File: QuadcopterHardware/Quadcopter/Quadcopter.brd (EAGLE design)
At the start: 3 x 47 mm, 47 parts, among them J2 FTDI_DEVICERA_SMT, M1 WIRELESS-NRF24L01, U1 ATMEGA328P_TQFP, U3 GY-521MPU6050

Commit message: more work on the board
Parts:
- C10, C11, C12, C13, C8: device rcl:C1206 -> rcl:C1210
- moved C2 115.4 mm to (38.7, 12.5)
- moved C1 113.1 mm to (43.0, 16.2), turned to 270 degrees
- moved MOSFET4 103.9 mm to (39.8, 3.59), turned to 180 degrees
- moved C13 100.8 mm to (38.2, 8.55)
- moved MOSFET3 89.2 mm to (31.1, 3.59), turned to 180 degrees
- moved C12 86.3 mm to (29.5, 8.55)
- moved C11 72.6 mm to (20.9, 8.55)
- moved C8 67.5 mm to (38.2, 22.1), turned to 90 degrees
- moved FLYBACK_DIODE4 51.8 mm to (34.1, 3.58), flipped to the bottom
- moved U3 48.8 mm to (24.4, 15.2), flipped to the bottom, turned to 270 degrees
- moved FLYBACK_DIODE3 46.9 mm to (25.6, 3.58), flipped to the bottom
- moved MOTOR3 46.6 mm to (36.2, 3.64)
- moved MOTOR2 41.9 mm to (27.6, 3.64)
- moved U$2 38.1 mm to (42.7, 21.2), turned to 180 degrees
- moved FLYBACK_DIODE2 31.8 mm to (16.8, 3.33), flipped to the bottom
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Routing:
- net GND: track 3.67 -> 30.8 mm, vias 0 -> 1
- net VBATT: track 9.88 -> 21.5 mm
- net XTAL2: track 4.49 -> 0.00 mm
- net XTAL1: track 3.88 -> 0.00 mm
- net 3V3: track 0.00 -> 3.03 mm
- net DRAIN3: track 3.32 -> 5.82 mm
- net AREF: track 2.89 -> 0.75 mm, vias 0 -> 1
- net DRAIN4: track 3.36 -> 2.32 mm
- net DRAIN1: track 6.85 -> 5.95 mm
- net DRAIN2: track 6.81 -> 6.07 mm
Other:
- board size 3 x 47 mm -> 47 x 28 mm

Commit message: more work on board
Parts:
- moved C6 76.6 mm to (5.15, 12.7), turned to 270 degrees
- moved R6 73.9 mm to (8.55, 12.0)
- moved S1 58.0 mm to (3.90, 7.15), turned to 270 degrees
- flipped J2 to the bottom, turned to 90 degrees
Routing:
- net AREF: track 0.75 -> 0.00 mm, vias 1 -> 0
- net GND: track 30.8 -> 30.3 mm, vias 1 -> 0
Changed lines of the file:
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@@
 <element name="C4" library="rcl" package="C0603" value="100nF" x="-41.91" y="57.15"/>
 <element name="C5" library="rcl" package="C0603" value="100nF" x="-49.53" y="57.15"/>
-<element name="C6" library="rcl" package="C0603" value="100nF" x="-57.15" y="57.15"/>
+<element name="C6" library="rcl" package="C0603" value="100nF" x="5.15" y="12.65" rot="R270"/>
 <element name="C7" library="rcl" package="C0603" value="100nF" x="30.85" y="16.73" rot="R90"/>
 <element name="C8" library="rcl" package="C1210" value="100uF" x="38.2" y="22.14" rot="R90"/>
@@
 <element name="FLYBACK_DIODE3" library="quad" package="MINI2-F3-B" value="DB2W40300L" x="25.6" y="3.58" rot="MR0"/>
 <element name="FLYBACK_DIODE4" library="quad" package="MINI2-F3-B" value="DB2W40300L" x="34.14" y="3.58" rot="MR0"/>
-<element name="J2" library="quad" package="FTDI_DEVICE_RA_SMT" value="FTDI_DEVICERA_SMT" x="-2.02" y="17.13" rot="R270">
-<attribute name="PROD_ID" value="CONN-08971" x="-2.02" y="17.13" size="1.778" layer="27" rot="R270" display="off"/>
+<element name="J2" library="quad" package="FTDI_DEVICE_RA_SMT" value="FTDI_DEVICERA_SMT" x="-2.02" y="17.12" rot="MR90">
+<attribute name="PROD_ID" value="CONN-08971" x="-2.02" y="17.12" size="1.778" layer="28" rot="MR90" display="off"/>
 </element>
 <element name="LED1" library="led" package="CHIP-LED0603" value="RED" x="85.76" y="25.92" rot="R270"/>
@@
 <element name="R3" library="rcl" package="R0603" value="150" x="88.91" y="22.58"/>
 <element name="R4" library="rcl" package="R0603" value="150" x="88.83" y="18.08"/>
-<element name="R6" library="rcl" package="R0603" value="10K" x="-44.45" y="63.5"/>
+<element name="R6" library="rcl" package="R0603" value="10K" x="8.55" y="12"/>
 <element name="R7" library="rcl" package="R0603" value="10K" x="-49.53" y="63.5"/>
 <element name="R8" library="rcl" package="R0603" value="1K" x="-30.48" y="68.58"/>
 <element name="R9" library="rcl" package="R0603" value="1.7K" x="-29.21" y="63.5"/>
 <element name="RES1" library="quad" package="CSTCE16M0V53-R0" value="CSTCE10M0G55-R0" x="31.03" y="9.63" rot="MR180"/>
-<element name="S1" library="quad" package="TACTILE-SWITCH-SMD" value="SWITCH-MOMENTARY-2SMD" x="-25.4" y="57.15">
-<attribute name="PROD_ID" value="SWCH-08247" x="-25.4" y="57.15" size="1.778" layer="27" display="off"/>
+<element name="S1" library="quad" package="TACTILE-SWITCH-SMD" value="SWITCH-MOMENTARY-2SMD" x="3.9" y="7.15" rot="R270">
+<attribute name="PROD_ID" value="SWCH-08247" x="3.9" y="7.15" size="1.778" layer="27" rot="R270" display="off"/>
 </element>
 <element name="U$1" library="quad" package="SOT95P270X145-5N" value="MCP1802T-3302I/OT" x="38.33" y="16.09" smashed="yes" rot="R180">
@@
 <wire x1="39.58" y1="12.5" x2="40.16" y2="12.5" width="1.016" layer="1"/>
 <wire x1="40.16" y1="12.5" x2="43" y2="15.34" width="1.016" layer="1"/>
-<wire x1="20.1574" y1="12.71" x2="30.48" y2="17.21" width="0" layer="19" extent="1-16"/>
-<wire x1="30.48" y1="17.21" x2="30.85" y2="17.58" width="0.4064" layer="1"/>
 <wire x1="13.67" y1="8.55" x2="13.67" y2="6.67" width="1.016" layer="1"/>
 <wire x1="13.67" y1="6.67" x2="13" y2="6" width="1.016" layer="1"/>
@@
 <wire x1="42.74" y1="22.2" x2="41.41" y2="16.09" width="0" layer="19" extent="1-1"/>
 <wire x1="30.93" y1="6.43" x2="39" y2="5.75" width="0" layer="19" extent="1-1"/>
-<wire x1="22.3" y1="6.8" x2="30.25" y2="5.75" width="0" layer="19" extent="1-1"/>
-<wire x1="31.03" y1="9.63" x2="22.3" y2="8.55" width="0" layer="19" extent="1-1"/>
-<wire x1="28.7426" y1="11.91" x2="31.03" y2="9.63" width="0" layer="19" extent="1-1"/>
-<wire x1="28.7426" y1="13.51" x2="28.7426" y2="11.91" width="0" layer="19" extent="1-1"/>
-<wire x1="18.04" y1="24.1" x2="28.7426" y2="13.51" width="0" layer="19" extent="1-1"/>
-<wire x1="13.67" y1="8.55" x2="31.03" y2="9.63" width="0" layer="19" extent="1-1"/>
-<wire x1="20.1574" y1="12.71" x2="28.7426" y2="11.91" width="0" layer="19" extent="1-1"/>
-<wire x1="8.63" y1="24.99" x2="18.04" y2="24.1" width="0" layer="19" extent="1-1"/>
-<wire x1="2.98" y1="10.78" x2="13.67" y2="8.55" width="0" layer="19" extent="1-1"/>
-<wire x1="2.98" y1="13.32" x2="2.98" y2="10.78" width="0" layer="19" extent="1-1"/>
-<wire x1="-16.93" y1="63.5" x2="8.63" y2="24.99" width="0" layer="19" extent="1-1"/>
+<wire x1="31.03" y1="9.63" x2="30.93" y2="8.55" width="0" layer="19" extent="1-16"/>
+<wire x1="28.7426" y1="11.91" x2="31.03" y2="9.63" width="0" layer="19" extent="16-16"/>
+<wire x1="28.7426" y1="13.51" x2="28.7426" y2="11.91" width="0" layer="19" extent="16-16"/>
+<wire x1="30.85" y1="17.58" x2="28.7426" y2="13.51" width="0" layer="19" extent="1-16"/>
+<wire x1="22.3" y1="8.55" x2="28.7426" y2="11.91" width="0" layer="19" extent="1-16"/>
+<wire x1="20.1574" y1="12.71" x2="22.3" y2="8.55" width="0" layer="19" extent="1-16"/>
+<wire x1="13.67" y1="8.55" x2="20.1574" y2="12.71" width="0" layer="19" extent="1-16"/>
+<wire x1="5.805" y1="9.944" x2="13.67" y2="8.55" width="0" layer="19" extent="1-1"/>
+<wire x1="2.98" y1="20.93" x2="5.805" y2="9.944" width="0" layer="19" extent="1-16"/>
+<wire x1="2.98" y1="23.47" x2="2.98" y2="20.93" width="0" layer="19" extent="16-16"/>
+<wire x1="8.63" y1="24.99" x2="2.98" y2="23.47" width="0" layer="19" extent="16-16"/>
+<wire x1="18.04" y1="24.1" x2="8.63" y2="24.99" width="0" layer="19" extent="1-1"/>
+<wire x1="-16.93" y1="63.5" x2="2.98" y2="23.47" width="0" layer="19" extent="1-16"/>
 <wire x1="-23.28" y1="63.5" x2="-16.93" y2="63.5" width="0" layer="19" extent="1-1"/>
-<wire x1="-28.194" y1="59.055" x2="-23.28" y2="63.5" width="0" layer="19" extent="1-1"/>
-<wire x1="-33.44" y1="57.15" x2="-28.194" y2="59.055" width="0" layer="19" extent="1-1"/>
-<wire x1="-35.14" y1="63.5" x2="-33.44" y2="57.15" width="0" layer="19" extent="1-1"/>
+<wire x1="-29.63" y1="68.58" x2="-23.28" y2="63.5" width="0" layer="19" extent="1-1"/>
+<wire x1="-35.14" y1="63.5" x2="-29.63" y2="68.58" width="0" layer="19" extent="1-1"/>
 <wire x1="-40.22" y1="63.5" x2="-35.14" y2="63.5" width="0" layer="19" extent="1-1"/>
 <wire x1="-41.06" y1="57.15" x2="-40.22" y2="63.5" width="0" layer="19" extent="1-1"/>
-<wire x1="-29.63" y1="68.58" x2="-35.14" y2="63.5" width="0" layer="19" extent="1-1"/>
+<wire x1="-33.44" y1="57.15" x2="-35.14" y2="63.5" width="0" layer="19" extent="1-1"/>
 <wire x1="-48.68" y1="57.15" x2="-41.06" y2="57.15" width="0" layer="19" extent="1-1"/>
 <wire x1="-50.38" y1="63.5" x2="-48.68" y2="57.15" width="0" layer="19" extent="1-1"/>
 <wire x1="-55.46" y1="63.5" x2="-50.38" y2="63.5" width="0" layer="19" extent="1-1"/>
-<via x="30.48" y="17.21" extent="1-16" drill="0.6" shape="square"/>
 </signal>
 <signal name="3V3">
@@
 <wire x1="-35.14" y1="57.15" x2="-24.98" y2="63.5" width="0" layer="19" extent="1-1"/>
 <wire x1="-42.76" y1="57.15" x2="-35.14" y2="57.15" width="0" layer="19" extent="1-1"/>
-<wire x1="-43.6" y1="63.5" x2="-42.76" y2="57.15" width="0" layer="19" extent="1-1"/>
+<wire x1="9.4" y1="12" x2="-42.76" y2="57.15" width="0" layer="19" extent="1-1"/>
 <wire x1="-50.38" y1="57.15" x2="-42.76" y2="57.15" width="0" layer="19" extent="1-1"/>
 <wire x1="11.17" y1="24.99" x2="-18.63" y2="63.5" width="0" layer="19" extent="1-1"/>
@@
 <wire x1="28.7426" y1="11.11" x2="28.7426" y2="12.71" width="0" layer="19" extent="1-1"/>
 <wire x1="20.1574" y1="10.31" x2="28.7426" y2="11.11" width="0" layer="19" extent="1-1"/>
-<wire x1="2.98" y1="15.86" x2="11.17" y2="24.99" width="0" layer="19" extent="1-1"/>
+<wire x1="2.98" y1="18.39" x2="11.17" y2="24.99" width="0" layer="19" extent="1-1"/>
 </signal>
 <signal name="RST">
@@
 <contactref element="C6" pad="1"/>
 <contactref element="R6" pad="1"/>
-<wire x1="-28.194" y1="55.245" x2="24.85" y2="16.6026" width="0" layer="19" extent="1-1"/>
-<wire x1="-45.3" y1="63.5" x2="-28.194" y2="55.245" width="0" layer="19" extent="1-1"/>
-<wire x1="-58" y1="57.15" x2="-45.3" y2="63.5" width="0" layer="19" extent="1-1"/>
+<wire x1="1.995" y1="9.944" x2="1.95" y2="9.944" width="0.4064" layer="1"/>
+<wire x1="7.7" y1="12" x2="24.85" y2="16.6026" width="0" layer="19" extent="1-16"/>
+<wire x1="5.15" y1="13.5" x2="7.7" y2="12" width="0" layer="19" extent="1-1"/>
+<wire x1="1.995" y1="9.944" x2="5.15" y2="13.5" width="0" layer="19" extent="1-1"/>
 </signal>
 <signal name="MISO">
@@
 <contactref element="U1" pad="31"/>
 <contactref element="J2" pad="2"/>
-<wire x1="2.98" y1="20.94" x2="26.45" y2="16.6026" width="0" layer="19" extent="1-1"/>
+<wire x1="2.98" y1="13.31" x2="26.45" y2="16.6026" width="0" layer="19" extent="1-1"/>
 </signal>
 <signal name="UART_RX">
 <contactref element="U1" pad="30"/>
 <contactref element="J2" pad="3"/>
-<wire x1="2.98" y1="18.4" x2="25.65" y2="16.6026" width="0" layer="19" extent="1-1"/>
+<wire x1="2.98" y1="15.85" x2="25.65" y2="16.6026" width="0" layer="19" extent="1-1"/>
 </signal>
 <signal name="SCL">
@@
 <contactref element="C6" pad="2"/>
 <contactref element="J2" pad="1"/>
-<wire x1="-56.3" y1="57.15" x2="2.98" y2="23.48" width="0" layer="19" extent="1-1"/>
+<wire x1="2.98" y1="10.77" x2="5.15" y2="11.8" width="0" layer="19" extent="1-16"/>
 </signal>
 <signal name="CSN">
@@
 <contactref element="U1" pad="20"/>
 <contactref element="C7" pad="1"/>
-<wire x1="20.1574" y1="11.91" x2="30.32" y2="16.41" width="0" layer="19" extent="1-16"/>
-<wire x1="30.32" y1="16.41" x2="30.85" y2="15.88" width="0.4064" layer="1"/>
-<via x="30.32" y="16.41" extent="1-16" drill="0.6" shape="square"/>
+<wire x1="20.1574" y1="11.91" x2="30.85" y2="15.88" width="0" layer="19" extent="1-16"/>
 </signal>
 <signal name="VDIV">

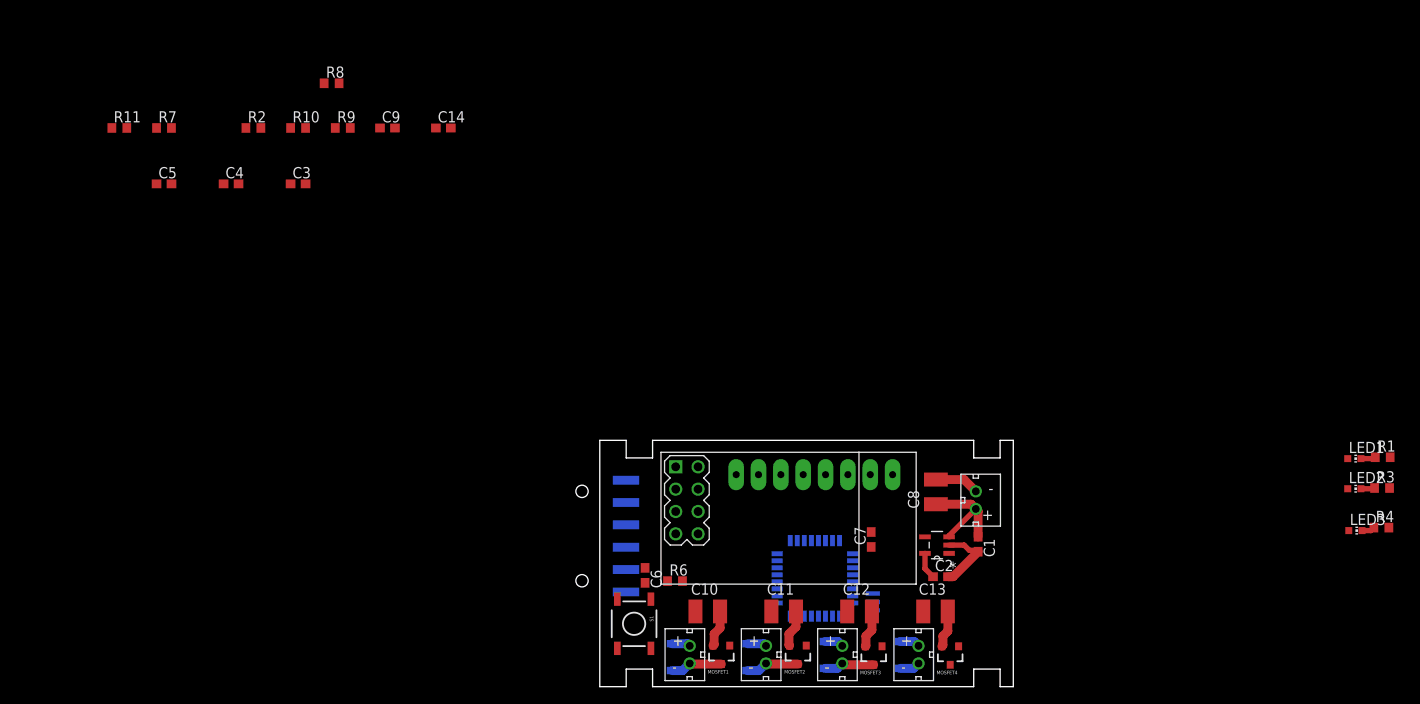
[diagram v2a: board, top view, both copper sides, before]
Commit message: Made some groups of components
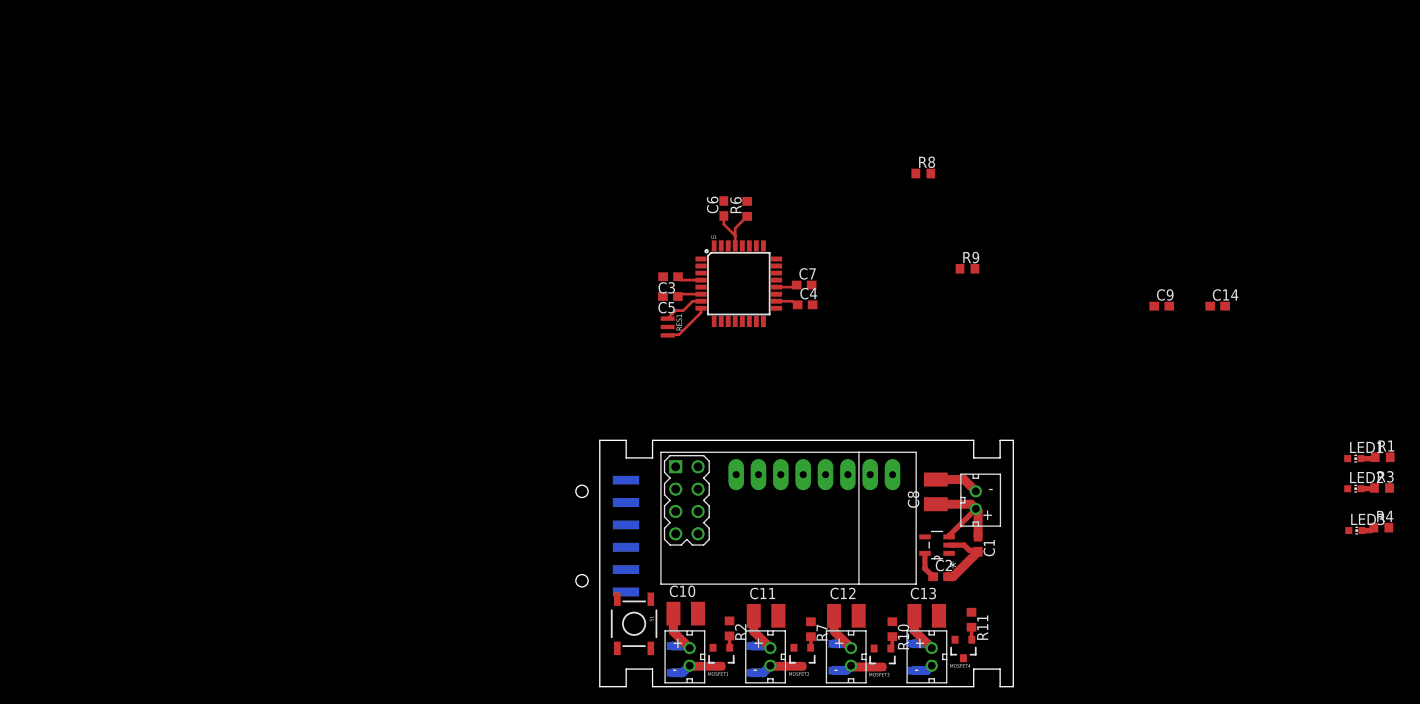
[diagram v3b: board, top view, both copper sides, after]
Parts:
- moved R11 111.8 mm to (42.2, 7.61), turned to 270 degrees
- moved R7 93.0 mm to (24.0, 6.53), turned to 270 degrees
- moved C14 90.3 mm to (70.2, 43.2)
- moved C9 90.3 mm to (63.9, 43.2)
- moved R10 88.4 mm to (33.2, 6.54), turned to 270 degrees
- moved R2 78.5 mm to (14.8, 6.62), turned to 270 degrees
- moved R9 72.8 mm to (41.8, 47.5)
- moved R8 68.0 mm to (36.8, 58.3)
- moved C4 66.7 mm to (23.3, 43.4)
- moved C5 59.0 mm to (8.03, 44.4), turned to 180 degrees
- moved C3 43.6 mm to (8.04, 46.6), turned to 180 degrees
- moved R6 43.1 mm to (16.8, 54.3), turned to 90 degrees
- moved C6 42.6 mm to (14.1, 54.4), turned to 90 degrees
- moved RES1 39.0 mm to (7.72, 40.9), flipped to the top
- moved U1 34.6 mm to (15.8, 45.8), flipped to the top
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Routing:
- net VBATT: track 21.5 -> 39.7 mm
- net GND: track 30.3 -> 13.3 mm
- net 3V3: track 3.03 -> 11.1 mm
- net RST: track 0.05 -> 6.74 mm
- net XTAL2: track 0.00 -> 5.36 mm
- net XTAL1: track 0.00 -> 4.61 mm
- net AREF: track 0.00 -> 2.87 mm
- net PWM4: track 0.00 -> 1.43 mm
- net PWM3: track 0.00 -> 1.42 mm
- net PWM1: track 0.00 -> 1.36 mm
- net PWM2: track 0.00 -> 1.27 mm

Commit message: did some more work on the PCB-added some polygons for GND and VBATT lines
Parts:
- moved R6 34.7 mm to (28.2, 21.5), turned to 180 degrees
- moved C6 33.4 mm to (19.1, 21.4), turned to 180 degrees
- moved RES1 31.3 mm to (19.0, 11.6), turned to 270 degrees
- moved C3 31.2 mm to (16.5, 16.6)
- moved C4 31.2 mm to (31.8, 13.4)
- moved C5 31.2 mm to (16.5, 14.3)
- moved C7 31.2 mm to (31.7, 15.7)
- moved U1 31.2 mm to (24.3, 15.8)
- moved C1 7.50 mm to (43.2, 23.7)
- moved C2 3.09 mm to (39.5, 15.5)
- moved U$2 2.51 mm to (43.0, 18.7)
- moved U$1 2.30 mm to (38.8, 18.3)
- moved U3 1.03 mm to (24.1, 16.2)
- moved C8 0.90 mm to (38.7, 22.9)
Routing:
- net VBATT: track 39.7 -> 67.4 mm
- net PWM4: track 1.43 -> 21.8 mm
- net ACC_INT: track 0.00 -> 16.3 mm
- net GND: track 13.3 -> 0.13 mm
- net SCL: track 0.00 -> 8.21 mm
- net PWM2: track 1.27 -> 8.40 mm
- net RST: track 6.74 -> 0.05 mm
- net SDA: track 0.00 -> 6.19 mm
- net DRAIN4: track 2.32 -> 6.28 mm
- net XTAL2: track 5.36 -> 1.42 mm
- net XTAL1: track 4.61 -> 3.56 mm
- net 3V3: track 11.1 -> 10.4 mm
- added copper zone on layer 1, net GND
- added copper zone on layer 16, net VBATT

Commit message: more work...
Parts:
- moved R6 4.78 mm to (33.0, 22.0)
- moved C6 3.09 mm to (16.1, 22.1)
- moved R11 2.25 mm to (42.2, 9.86)
- moved C13 1.75 mm to (37.2, 9.80)
- moved FLYBACK_DIODE4 1.50 mm to (35.6, 4.83)
- moved MOTOR3 1.50 mm to (37.7, 4.89)
- moved MOSFET4 1.00 mm to (41.3, 5.34)
- moved C1 0.75 mm to (43.2, 22.9)
- moved C3 0.75 mm to (16.5, 17.4)
- moved C4 0.75 mm to (31.8, 14.2)
- moved C5 0.75 mm to (16.5, 15.1)
- moved M1 0.75 mm to (21.3, 19.4)
- moved RES1 0.75 mm to (19.0, 12.4)
- moved U3 0.75 mm to (23.4, 16.2)
- moved C7 0.75 mm to (31.7, 16.4)
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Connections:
- net PWM1: now also U1.9; no longer U1.1
- net PWM2: now also U1.10; no longer U1.9
- net PWM3: now also U1.13; no longer U1.10
- net PWM4: now also U1.14; no longer U1.13
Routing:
- net ACC_INT: track 16.3 -> 0.00 mm
- net PWM1: track 1.36 -> 15.9 mm
- net PWM3: track 1.42 -> 14.6 mm
- net SCL: track 8.21 -> 0.00 mm
- net SDA: track 6.19 -> 0.00 mm
- net PWM4: track 21.8 -> 22.5 mm

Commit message: more work
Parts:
- moved C13 0.25 mm to (37.2, 9.55)
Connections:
- net CE: now also U1.2; no longer U1.12
- net CSN: now also U1.1; no longer U1.2
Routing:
- net 3V3: track 10.4 -> 64.9 mm, vias 0 -> 2
- net GND: track 0.13 -> 36.3 mm, vias 0 -> 3
- net MISO: track 0.00 -> 24.1 mm, vias 0 -> 1
- net MOSI: track 0.00 -> 23.9 mm, vias 0 -> 1
- net CE: track 0.00 -> 13.3 mm
- net CSN: track 0.00 -> 10.8 mm
- added copper zone on layer 16, net GND
